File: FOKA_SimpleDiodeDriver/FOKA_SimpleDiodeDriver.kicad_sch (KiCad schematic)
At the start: 22 parts, among them J1 IN, J2 Conn_01x02, Q2 BJT, U2 ADA4891-1

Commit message: v0.9
awaiting pre-production review
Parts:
- J2: footprint Power_Connectors:691311500102 -> Power_Connectors:691313510002
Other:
- company: (none) -> KN FOKA
- title: (none) -> Zabezpieczony sterownik diody IR
- moved on the sheet: C1, C2, D1, D2, D3A, D3B, D4, D5, D6, D7, J1, J2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

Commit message: minor updates
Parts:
- removed D4: 2V5, Diode_SMD:D_SOD-323_HandSoldering, symbol Device:D_Zener
- added C3: 1u, Capacitor_SMD:C_0603_1608Metric_Pad1.08x0.95mm_HandSolder, symbol Device:C_Small
- added C4: 10p, Capacitor_SMD:C_0603_1608Metric_Pad1.08x0.95mm_HandSolder, symbol Device:C_Small
- added R6: 10k, symbol Device:R_Small
- added R7: 15k, symbol Device:R_Small
- added U1: AZ431L, Package_TO_SOT_SMD:SOT-23, symbol Reference_Voltage:TL432DBZ
- C1: value 1u -> 10u
- C2: value 100n -> 1u
- D1: value LED -> IR LED
- R2: value R -> 3k
- R3, R4, R5: value R -> 1k5
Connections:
- net GND: now also C3.2, C4.2, R7.2, U1.3 (A)
- net at D3.2 (K), R2.2: now also C3.1, R6.1, U1.2 (K)
- net at D3.3 (K), D3.3 (K), R3.2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: now also C4.1
- new net: R6.2, R7.1, U1.1 (REF)
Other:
- note added: "ESD prot"
- note added: "SIGNAL OV/LED OC protection"
- note added: "filtering optional"
- note added: "high precision"
- note added: "if needed"
- note added: "precision"
- note added: "~2.1V from regulator"
- moved on the sheet: C1, C2, D1, D2, D5, D6, D7, J1, J2, Q2, R1, R2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

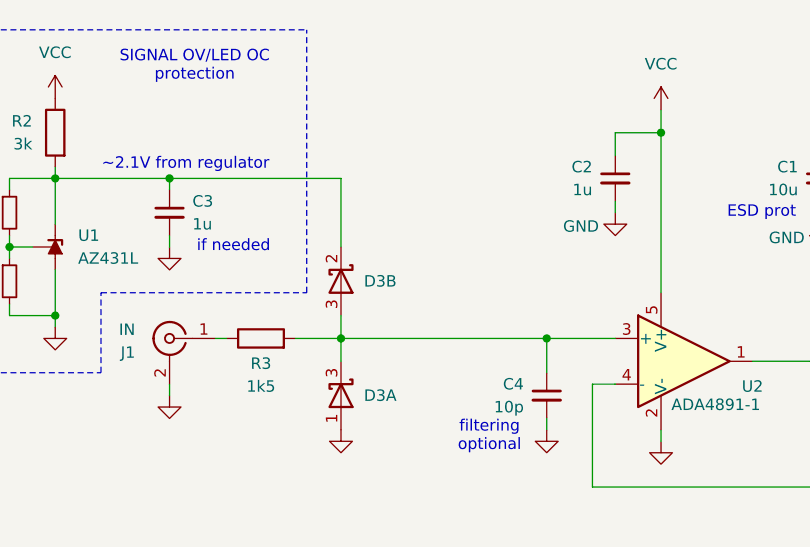
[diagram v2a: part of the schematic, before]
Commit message: recommended changes
voltage reference as OC prot.
layout changes
made vias bigger
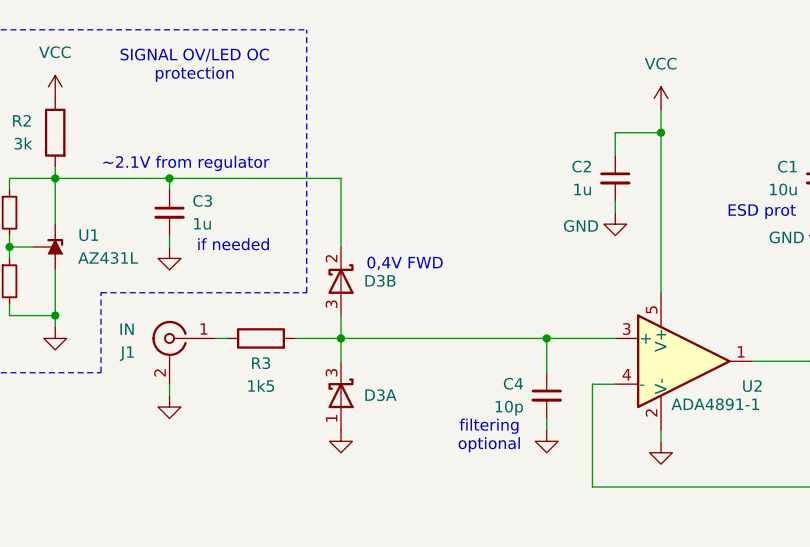
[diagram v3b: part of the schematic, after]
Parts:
- R6, R7: footprint (none) -> Resistor_SMD:R_0603_1608Metric_Pad0.98x0.95mm_HandSolder
- U1: footprint Package_TO_SOT_SMD:SOT-23 -> Package_TO_SOT_SMD:SOT-23-3
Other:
- note added: "0,4V FWD"
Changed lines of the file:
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@@
 		)
 	)
+	(text "0,4V FWD"
+		(exclude_from_sim no)
+		(at 135.382 89.662 0)
+		(effects
+			(font
+				(size 1.27 1.27)
+			)
+		)
+	)
 	(text "filtering\noptional"
 		(exclude_from_sim no)
@@
 			)
 		)
-		(property "Footprint" "Package_TO_SOT_SMD:SOT-23"
+		(property "Footprint" "Package_TO_SOT_SMD:SOT-23-3"
 			(at 100.838 87.63 0)
 			(effects
@@
 	)
 	(symbol
+		(lib_id "Device:R_Small")
+		(at 91.44 91.44 0)
+		(unit 1)
+		(exclude_from_sim no)
+		(in_bom yes)
+		(on_board yes)
+		(dnp no)
+		(property "Reference" "R7"
+			(at 88.9 90.1699 0)
+			(effects
+				(font
+					(size 1.016 1.016)
+				)
+				(justify right)
+			)
+		)
+		(property "Value" "15k"
+			(at 88.9 92.7099 0)
+			(effects
+				(font
+					(size 1.27 1.27)
+				)
+				(justify right)
+			)
+		)
+		(property "Footprint" "Resistor_SMD:R_0603_1608Metric_Pad0.98x0.95mm_HandSolder"
+			(at 91.44 91.44 0)
+			(effects
+				(font
+					(size 1.27 1.27)
+				)
+				(hide yes)
+			)
+		)
+		(property "Datasheet" "~"
+			(at 91.44 91.44 0)
+			(effects
+				(font
+					(size 1.27 1.27)
+				)
+				(hide yes)
+			)
+		)
+		(property "Description" "Resistor, small symbol"
+			(at 91.44 91.44 0)
+			(effects
+				(font
+					(size 1.27 1.27)
+				)
+				(hide yes)
+			)
+		)
+		(pin "1"
+		)
+		(pin "2"
+		)
+		(instances
+			(project "FOKA_SimpleDiodeDriver"
+				(path "/06dea30e-cb94-4d69-b691-0bfb7fef4029"
+					(reference "R7")
+					(unit 1)
+				)
+			)
+		)
+	)
+	(symbol
 		(lib_id "power:GND")
 		(at 237.49 148.59 0)
@@
 			)
 		)
-		(property "Footprint" ""
+		(property "Footprint" "Resistor_SMD:R_0603_1608Metric_Pad0.98x0.95mm_HandSolder"
 			(at 91.44 83.82 0)
 			(effects
@@
 					(unit 1)
 				)
-			)
-		)
-	)
-	(symbol
-		(lib_id "Device:R_Small")
-		(at 91.44 91.44 0)
-		(unit 1)
-		(exclude_from_sim no)
-		(in_bom yes)
-		(on_board yes)
-		(dnp no)
-		(property "Reference" "R7"
-			(at 88.9 90.1699 0)
-			(effects
-				(font
-					(size 1.016 1.016)
-				)
-				(justify right)
-			)
-		)
-		(property "Value" "15k"
-			(at 88.9 92.7099 0)
-			(effects
-				(font
-					(size 1.27 1.27)
-				)
-				(justify right)
-			)
-		)
-		(property "Footprint" ""
-			(at 91.44 91.44 0)
-			(effects
-				(font
-					(size 1.27 1.27)
-				)
-				(hide yes)
-			)
-		)
-		(property "Datasheet" "~"
-			(at 91.44 91.44 0)
-			(effects
-				(font
-					(size 1.27 1.27)
-				)
-				(hide yes)
-			)
-		)
-		(property "Description" "Resistor, small symbol"
-			(at 91.44 91.44 0)
-			(effects
-				(font
-					(size 1.27 1.27)
-				)
-				(hide yes)
-			)
-		)
-		(pin "1"
-		)
-		(pin "2"
-		)
-		(instances
-			(project "FOKA_SimpleDiodeDriver"
-				(path "/06dea30e-cb94-4d69-b691-0bfb7fef4029"
-					(reference "R7")
-					(unit 1)
-				)

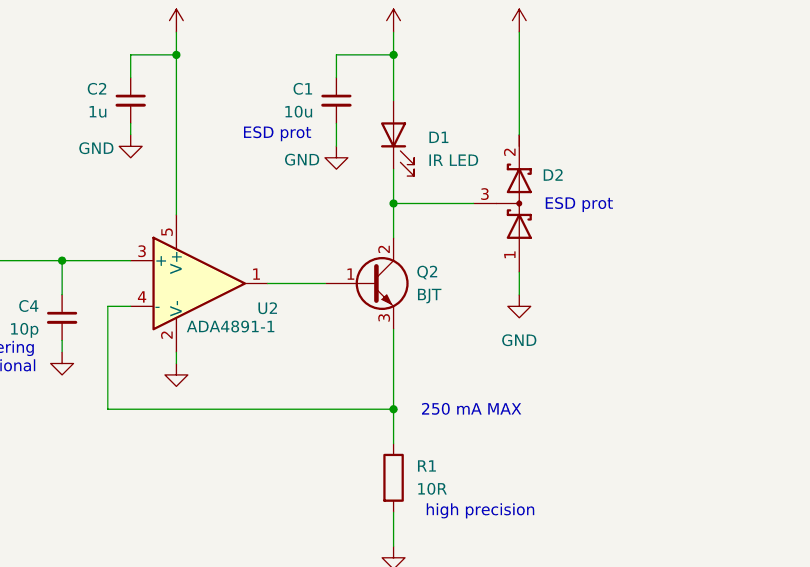
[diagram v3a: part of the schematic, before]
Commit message: BJT -> NMOS
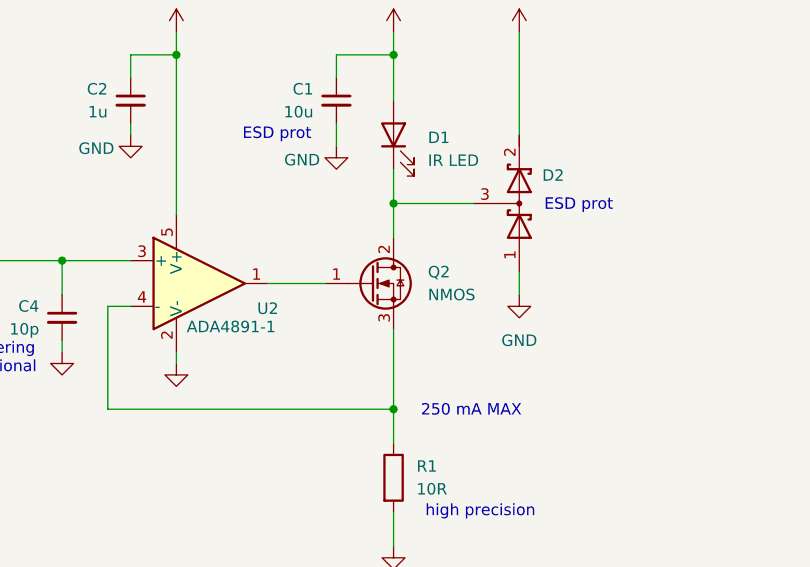
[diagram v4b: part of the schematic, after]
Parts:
- Q2: value BJT -> NMOS; symbol Device:Q_NPN_BCE -> Transistor_FET:Q_NMOS_GDS
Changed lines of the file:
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@@
 	)
 	(symbol
-		(lib_id "Device:Q_NPN_BCE")
+		(lib_id "Transistor_FET:Q_NMOS_GDS")
 		(at 185.42 100.33 0)
 		(unit 1)
@@
 		(fields_autoplaced yes)
 		(property "Reference" "Q2"
-			(at 190.5 99.0599 0)
+			(at 191.77 99.0599 0)
 			(effects
 				(font
@@
 			)
 		)
-		(property "Value" "BJT"
-			(at 190.5 101.5999 0)
+		(property "Value" "NMOS"
+			(at 191.77 101.5999 0)
 			(effects
 				(font
@@
 			)
 		)
-		(property "Description" "NPN transistor, base/collector/emitter"
+		(property "Description" "N-MOSFET transistor, gate/drain/source"
 			(at 185.42 100.33 0)
 			(effects

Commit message: Humpback update drop
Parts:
- added R8: 1M, Resistor_SMD:R_0603_1608Metric_Pad0.98x0.95mm_HandSolder, symbol Device:R
- R1: value 10R -> 1R
- R3: value 1k5 -> 100
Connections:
- net GND: now also R8.2
- net at C4.1, D3.3 (K), D3.3 (K)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: now also R8.1
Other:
- moved on the sheet: C1, C2, C4, D1, D2, Q2, R1, U2

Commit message: Final?
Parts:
- added C5: optional, Capacitor_SMD:C_0402_1005Metric, symbol Device:C_Small
- added R9: optional, Capacitor_SMD:C_0402_1005Metric, symbol Device:R
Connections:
- net GND: now also C5.1
- net at Q2.3 (S), R1.1: now also R9.2; no longer U2.4 (-)
- new net: C5.2, R9.1, U2.4 (-)

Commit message: RezystorDoBramki
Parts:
- added R10: optional, Capacitor_SMD:C_0402_1005Metric, symbol Device:R
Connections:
- net at Q2.1 (G): now also R10.2; no longer U2.1
- new net: R10.1, U2.1
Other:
- moved on the sheet: C1, D1, D2, Q2, R1, R9
